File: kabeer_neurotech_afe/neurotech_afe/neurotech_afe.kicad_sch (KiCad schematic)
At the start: 29 parts, among them J2 Conn_01x03_Socket, U2 Opamp_Quad, U3 ${SIM.PARAMS}

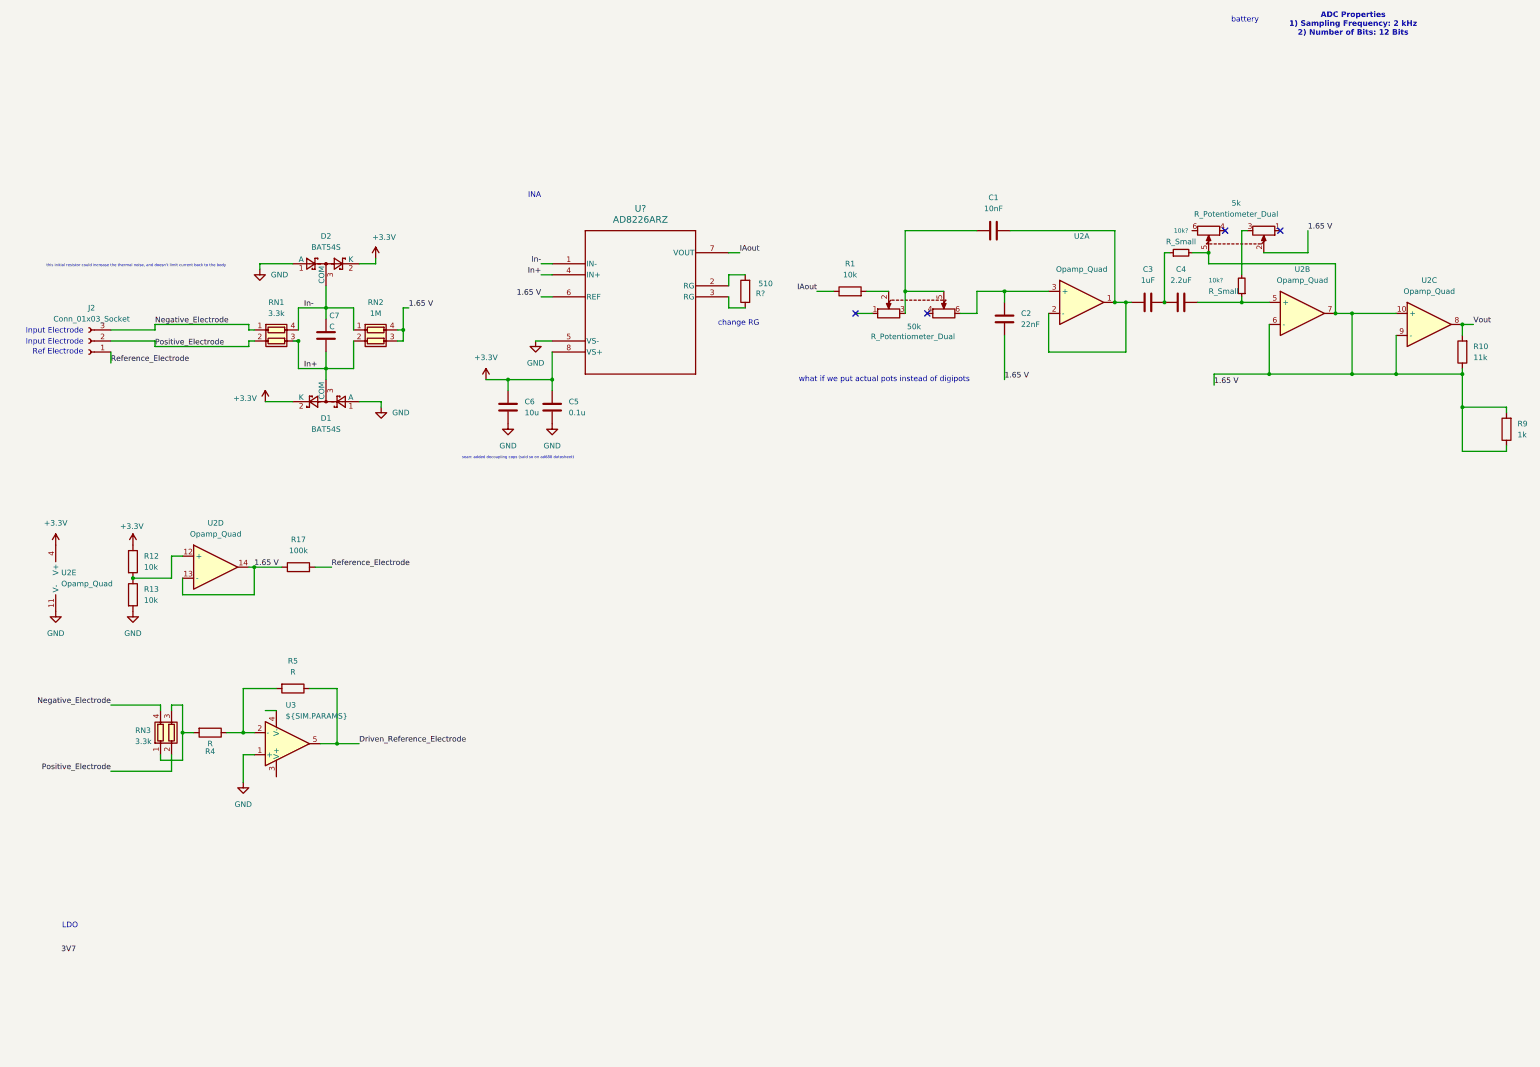
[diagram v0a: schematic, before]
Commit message: Added LDO voltage stepdown from 3.3 --> 3.7 and basic connections to ADS
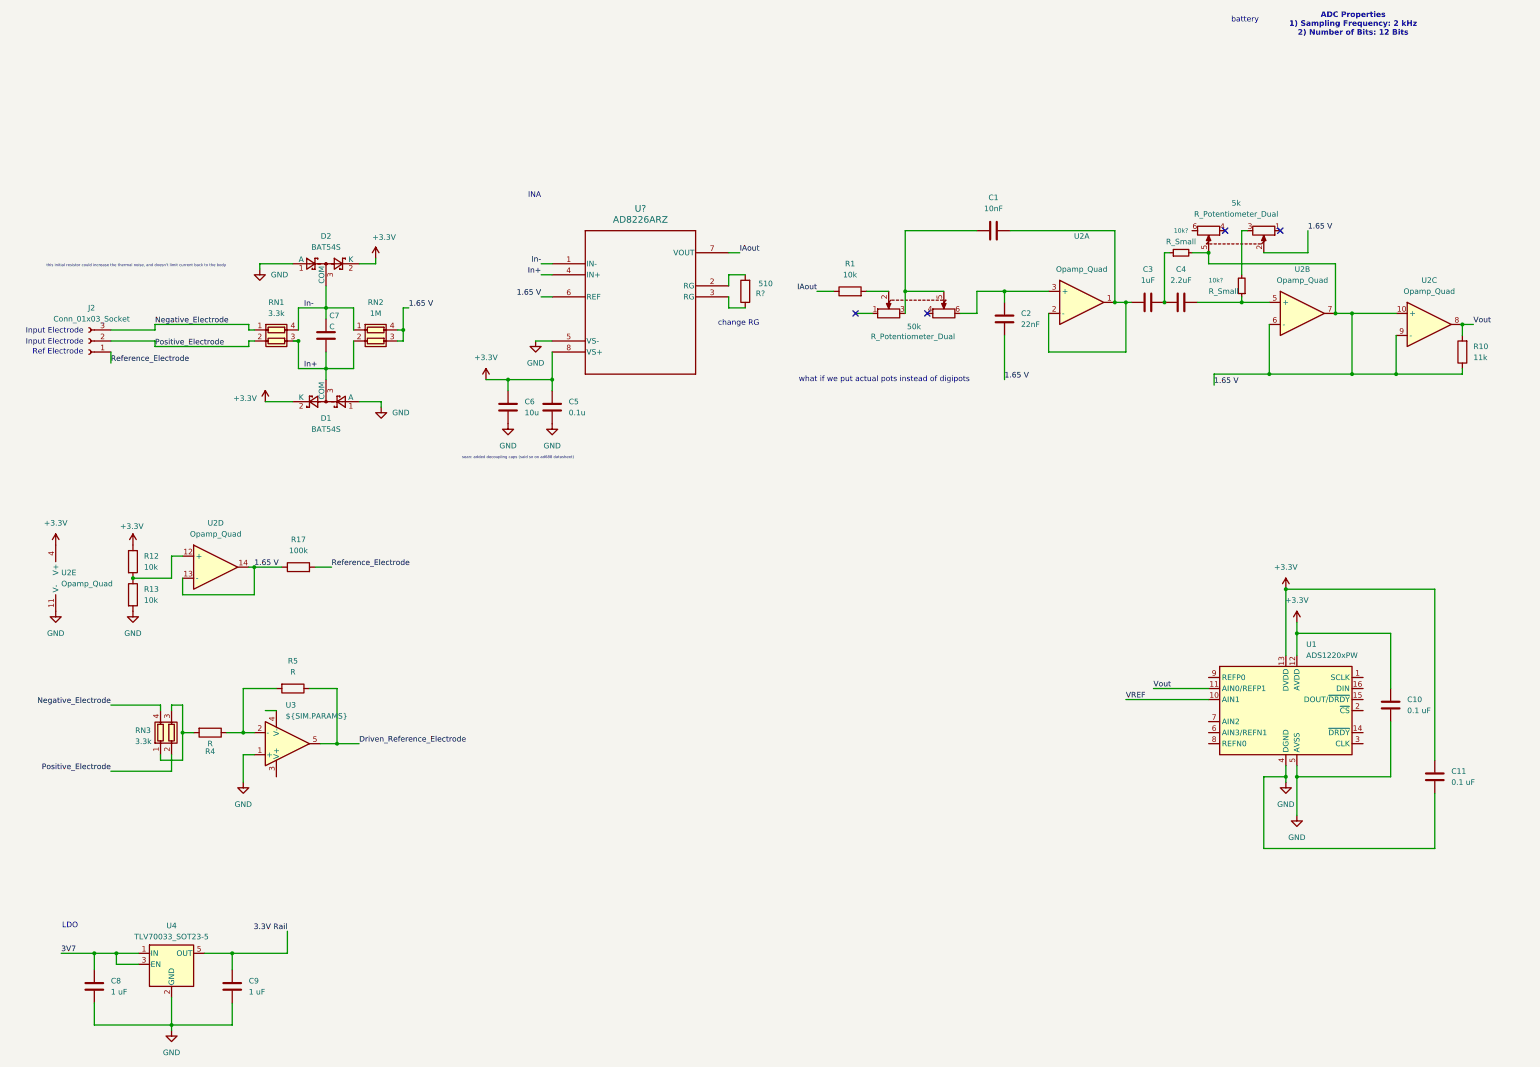
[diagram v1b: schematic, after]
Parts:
- removed R9: 1k, symbol Device:R
- added C10, C11: 0.1 uF, symbol Device:C
- added C8, C9: 1 uF, symbol Device:C
- added U1: ADS1220xPW, Package_SO:TSSOP-16_4.4x5mm_P0.65mm, symbol Analog_ADC:ADS1220xPW
- added U4: TLV70033_SOT23-5, Package_TO_SOT_SMD:SOT-23-5, symbol Regulator_Linear:TLV70033_SOT23-5
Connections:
- net +3.3V: now also C10.1, C11.1, U1.12 (AVDD), U1.13 (DVDD)
- net 3V7: now also C8.1, U4.1 (IN), U4.3 (EN)
- net GND: now also C10.2, C11.2, C8.2, C9.2, U1.4 (DGND), U1.5 (AVSS), U4.2 (GND)
- net Vout: now also U1.11 (AIN0/REFP1)
- new net 3.3V Rail: C9.1, U4.5 (OUT)
- new net VREF: U1.10 (AIN1)

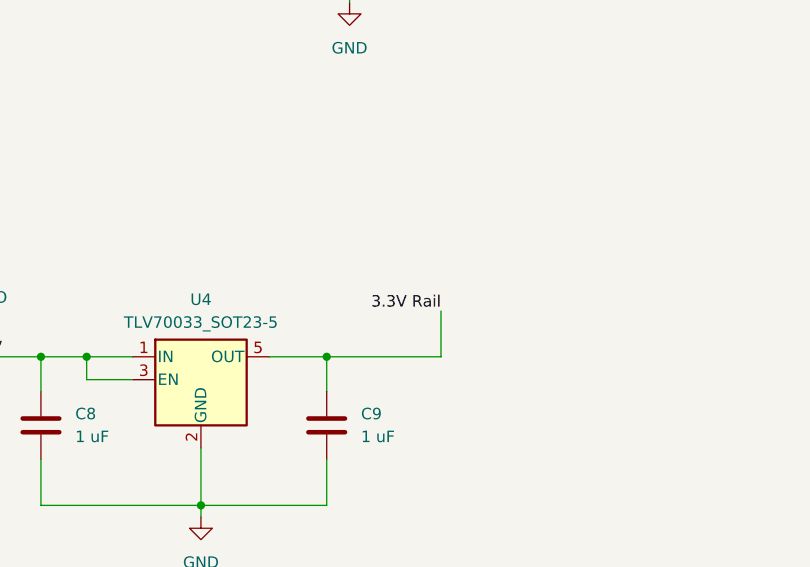
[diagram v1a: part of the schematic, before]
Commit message: changed ldo output power rail to 3.3V flag
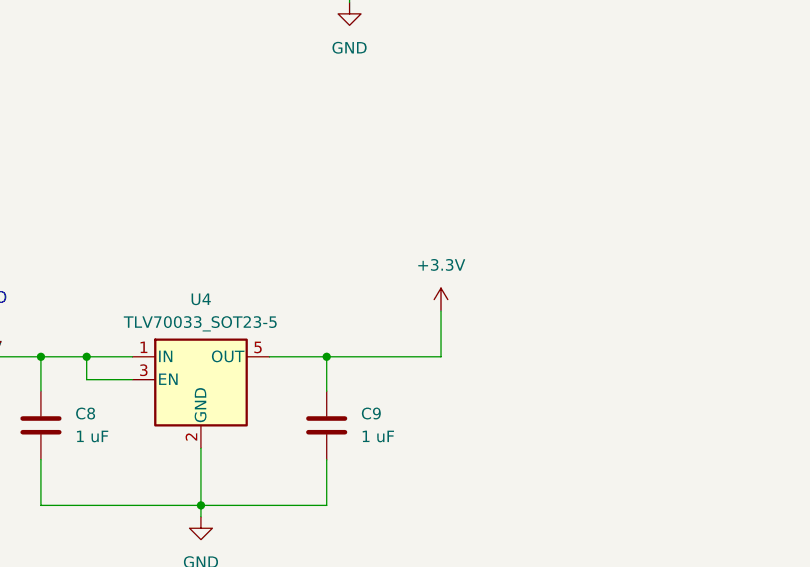
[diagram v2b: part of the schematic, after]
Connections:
- net 3.3V Rail is gone; now on net +3.3V: C9.1, U4.5 (OUT)
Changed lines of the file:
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@@
-		)
-	)
-	(label "3.3V Rail"
-		(at 77.47 191.77 180)
-		(effects
-			(font
-				(size 1.27 1.27)
-			)
-			(justify right bottom)
 		)
 	)
@@
 					(unit 1)
 				)
+			)
+		)
+	)
+	(symbol
+		(lib_id "power:+3.3V")
+		(at 77.47 191.77 0)
+		(unit 1)
+		(exclude_from_sim no)
+		(in_bom yes)
+		(on_board yes)
+		(dnp no)
+		(fields_autoplaced yes)
+		(property "Reference" "#PWR019"
+			(at 77.47 195.58 0)
+			(effects
+				(font
+					(size 1.27 1.27)
+				)
+				(hide yes)
+			)
+		)
+		(property "Value" "+3.3V"
+			(at 77.47 186.69 0)
+			(effects
+				(font
+					(size 1.27 1.27)
+				)
+			)
+		)
+		(property "Footprint" ""
+			(at 77.47 191.77 0)
+			(effects
+				(font
+					(size 1.27 1.27)
+				)
+				(hide yes)
+			)
+		)
+		(property "Datasheet" ""
+			(at 77.47 191.77 0)
+			(effects
+				(font
+					(size 1.27 1.27)
+				)
+				(hide yes)
+			)
+		)
+		(property "Description" "Power symbol creates a global label with name \"+3.3V\""
+			(at 77.47 191.77 0)
+			(effects
+				(font
+					(size 1.27 1.27)
+				)
+				(hide yes)
+			)
+		)
+		(pin "1"
+		)
+		(instances
+			(project ""
+				(path "/d657415d-773f-4d61-9200-85fede9d1019"
+					(reference "#PWR019")
+					(unit 1)
+				)
